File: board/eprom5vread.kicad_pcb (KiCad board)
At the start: 4 copper layers, 47 parts, among them J1 Barrel_Jack, J2 Conn_02x21_Counter_Clockwise, U1 NCP1117ST33T3G, U2 NCP1117ST50T3G, U3 TXB0108PW, U4 TXB0108PW, U5 TXB0108PW, U6 TXB0108PW, U7 TXB0108PW, U8 STM32G0B0CETx

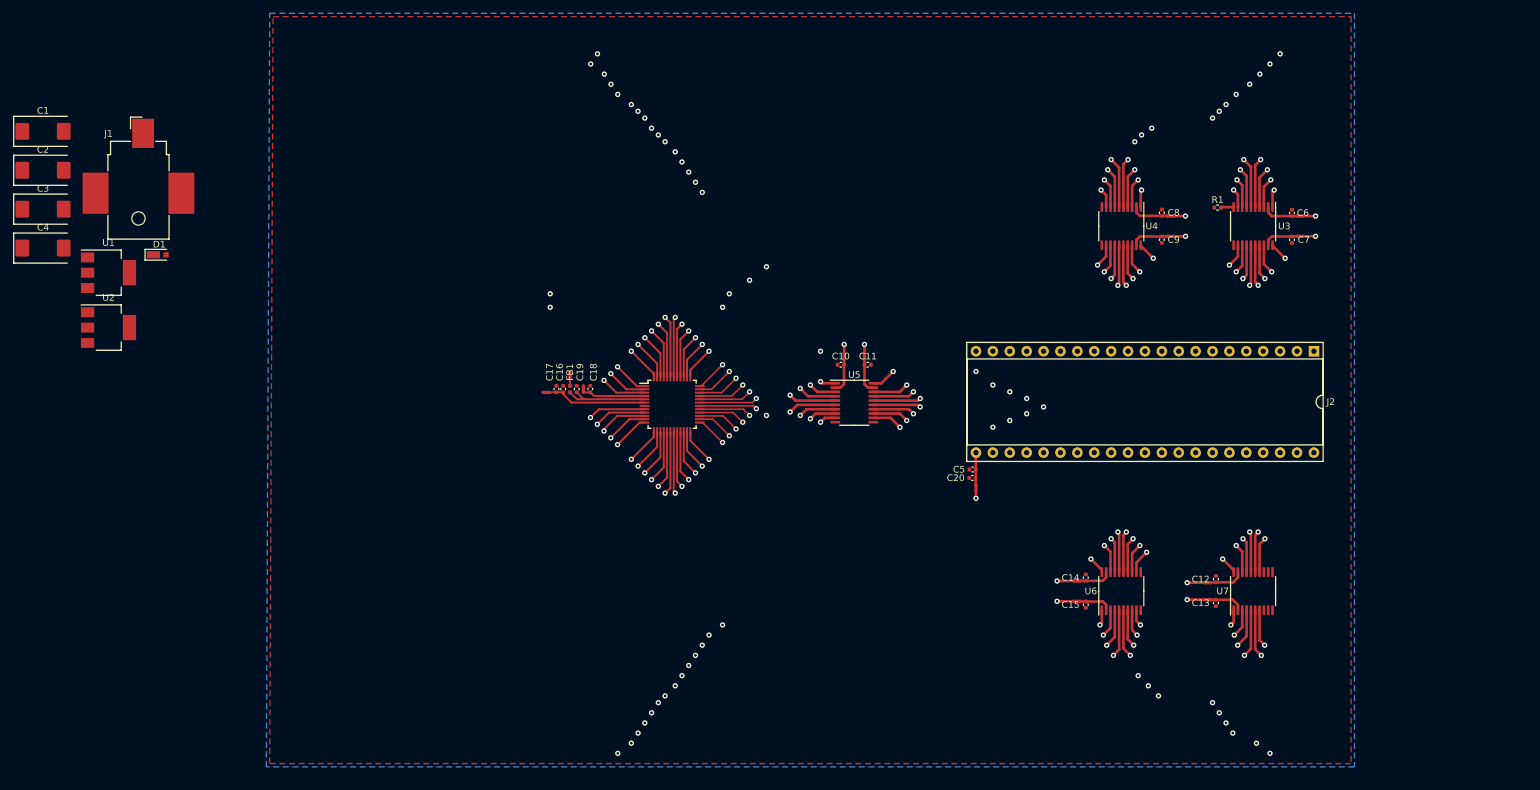
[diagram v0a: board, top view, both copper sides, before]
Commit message: initial board layout (WIP), schematic tuning
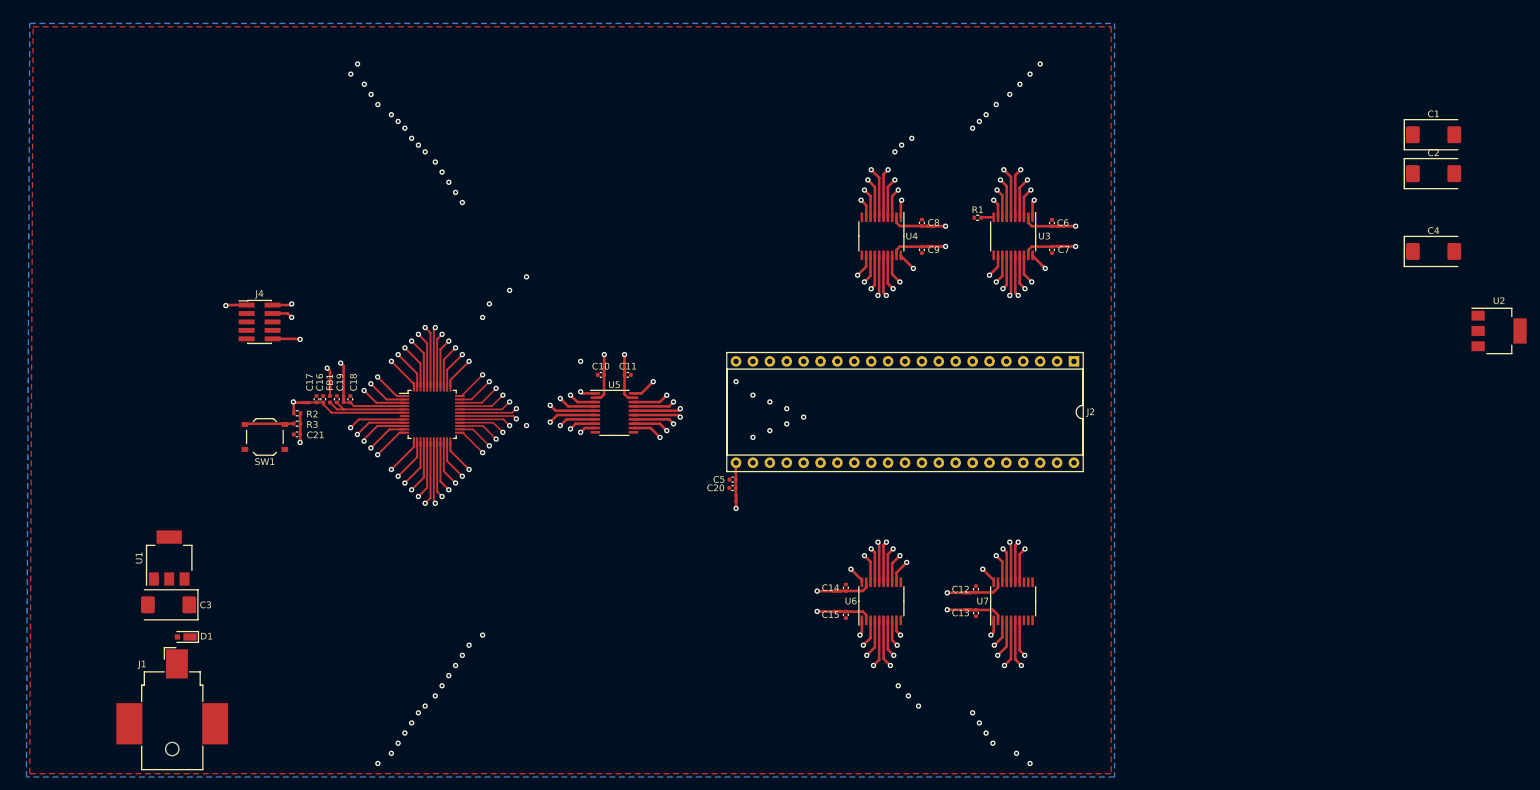
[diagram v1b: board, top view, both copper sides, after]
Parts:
- added C21: 100nF, Capacitor_SMD:C_0402_1005Metric, F.Cu at (83.3, 88.2)
- added J4: DEBUG, Connector_PinHeader_1.27mm:PinHeader_2x05_P1.27mm_Vertical_SMD, F.Cu at (77.7, 71.3)
- added R2: 2.2kΩ, Resistor_SMD:R_0402_1005Metric, F.Cu at (83.4, 85.0)
- added R3: 330Ω, Resistor_SMD:R_0402_1005Metric, F.Cu at (83.4, 86.6)
- added SW1: RST, Button_Switch_SMD:SW_Push_1P1T_XKB_TS-1187A, F.Cu at (78.5, 88.6)
- moved C1 209.0 mm to (254.2, 43.1)
- moved C2 209.0 mm to (254.2, 49.0)
- moved C4 209.0 mm to (254.2, 60.7)
- moved U2 209.0 mm to (264.1, 72.6)
- moved J1 79.9 mm to (64.6, 128.5)
- moved C3 62.4 mm to (64.0, 113.8), turned to 180 degrees
- moved D1 57.6 mm to (66.4, 118.6), turned to 180 degrees
- moved U1 43.9 mm to (64.1, 106.8), turned to 90 degrees
- moved C12 36.1 mm to (185.4, 111.5)
- moved C13 36.1 mm to (185.4, 115.1)
- moved C14 36.1 mm to (165.9, 111.3)
- moved C15 36.1 mm to (165.9, 115.3)
- moved C16 36.1 mm to (87.3, 82.9)
- moved C5 36.1 mm to (148.8, 95.0)
- moved C6 36.1 mm to (196.8, 56.4)
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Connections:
- C2 pad 1: /Power Supply/+3.3V -> /EPROM/+3.3V
- C4 pad 1: /Power Supply/+5V -> /EPROM/+5V
- NT1 pad 1: /MCU/+3.3V -> /EPROM/+3.3V
- NT2 pad 1: /MCU/+3.3V -> /EPROM/+3.3V
- NT3 pad 1: /MCU/+3.3V -> /EPROM/+3.3V
- U1 pad 2: /Power Supply/+3.3V -> /EPROM/+3.3V
- U2 pad 2: /Power Supply/+5V -> /EPROM/+5V
- U8 pad 10: unconnected-(U8-NRST-Pad10) -> /MCU/MCU Debug/~{RST}
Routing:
- net /MCU/MCU Debug/~{RST}: track 0.00 -> 40.9 mm, vias 0 -> 3
- net /EPROM/+3.3V: track 9.95 -> 23.8 mm, vias 5 -> 9
- net Net-(R3-Pad2): track 0.00 -> 7.22 mm
- net unconnected-(U8-NRST-Pad10): track 7.18 -> 0.00 mm, vias 1 -> 0
- net /MCU/SWCLK: track 39.3 -> 45.2 mm
- net /MCU/SWDIO: track 44.2 -> 49.9 mm

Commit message: finish board design
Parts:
- added J102: UART, Connector_PinHeader_2.54mm:PinHeader_2x01_P2.54mm_Vertical_SMD, F.Cu at (77.8, 58.1)
- added NT301: NetTie_2, NetTie:NetTie-2_SMD_Pad0.5mm, F.Cu at (61.5, 95.5)
- added NT302: NetTie_2, NetTie:NetTie-2_SMD_Pad0.5mm, F.Cu at (75.7, 99.1)
- added REF1: JLCPCB_Mounting_Hole, JLCPCB:JLCPCB_Mounting_Hole, F.Cu at (49.5, 32.0)
- added REF2: JLCPCB_Mounting_Hole, JLCPCB:JLCPCB_Mounting_Hole, F.Cu at (200.7, 32.0)
- added REF3: JLCPCB_Mounting_Hole, JLCPCB:JLCPCB_Mounting_Hole, F.Cu at (49.5, 134.1)
- added REF4: Polarity_Center_Positive_6mm_SilkScreen, Symbol:Polarity_Center_Positive_6mm_SilkScreen, F.Cu at (86.9, 124.2)
- moved C301 208.6 mm to (58.2, 114.6), turned to 180 degrees
- moved C302 202.3 mm to (58.2, 99.1), turned to 180 degrees
- moved U302 196.8 mm to (70.2, 106.8), turned to 90 degrees
- moved C304 188.0 mm to (70.1, 99.1), turned to 180 degrees
- moved C303 6.14 mm to (70.1, 114.6)
- moved U301 5.84 mm to (58.3, 106.8)
- moved R201 1.52 mm to (184.2, 55.6)
- renumbered C17 to C101, C16 to C102, C18 to C103, C19 to C104, C21 to C105, C6 to C201, C7 to C202, C8 to C203, C9 to C204, C10 to C205, C11 to C206, C15 to C207, C14 to C208, C13 to C209, C12 to C210, C20 to C211, C5 to C212, C1 to C301, C2 to C302, C3 to C303, C4 to C304, D1 to D301, FB1 to FB101, J4 to J101, J2 to J201, J1 to J301, NT1 to NT101, NT2 to NT102, NT3 to NT103, NT4 to NT201, NT9 to NT202, NT5 to NT203, NT10 to NT204, NT6 to NT205, NT11 to NT206, NT12 to NT207, NT8 to NT208, NT13 to NT209, NT7 to NT210, R2 to R101, R3 to R102, R1 to R201, SW1 to SW101, U8 to U101, U3 to U201, U4 to U202, U5 to U203, U6 to U204, U7 to U205, U1 to U301, U2 to U302
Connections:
- C302 pad 1: /EPROM/+3.3V -> Net-(U301-VO)
- C304 pad 1: /EPROM/+5V -> Net-(U302-VO)
- U101 pad 11: /MCU/PA0 -> /LSOE
- U301 pad 2: /EPROM/+3.3V -> Net-(U301-VO)
- U302 pad 2: /EPROM/+5V -> Net-(U302-VO)
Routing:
- net /LSOE: track 1.93 -> 264.1 mm, vias 0 -> 9
- net /EPROM/+5V: track 11.0 -> 69.5 mm, vias 6 -> 8
- net /MCU/UART_MCUTX: track 32.8 -> 82.1 mm, vias 3 -> 4
- net /MCU/UART_MCURX: track 24.7 -> 68.1 mm, vias 2 -> 3
- net Net-(D301-K): track 0.00 -> 25.2 mm
- net Net-(U301-VO): track 0.00 -> 15.2 mm
- net Net-(U302-VO): track 0.00 -> 14.0 mm
- net /MCU/PA0: track 6.21 -> 0.00 mm, vias 1 -> 0
- net Net-(D301-A): track 0.00 -> 3.97 mm
- net /EPROM/+3.3V: track 23.8 -> 25.3 mm, vias 9 -> 10
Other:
- board outline added: 161 x 112 mm
- board text added: "+3.3V"
- board text added: "+5V"
- board text added: "12V recommended"
- board text added: "EPROM 5V Read"
- board text added: "UART +3.3V"
- board text added: "r0001"
- board text added: "←MCU"
- board text added: "→MCU"

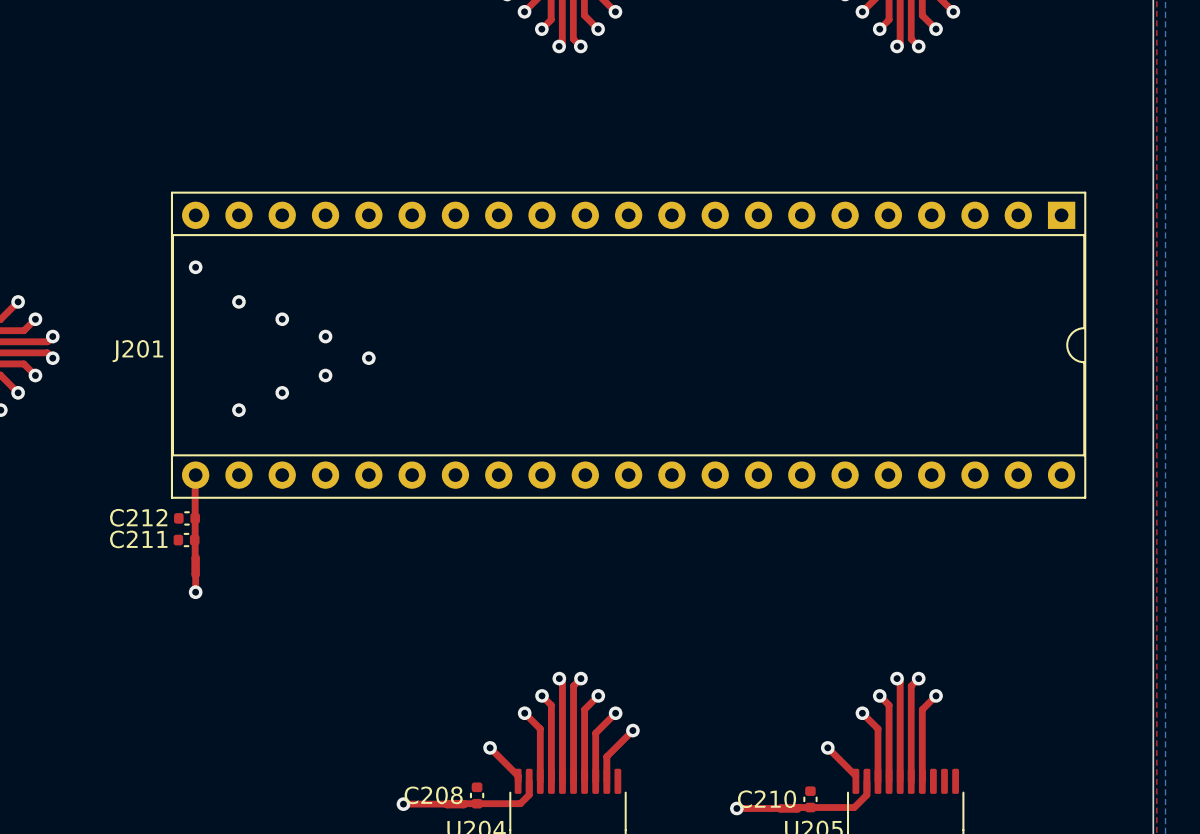
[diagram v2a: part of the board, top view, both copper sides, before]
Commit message: pcb: add ROM pin hints
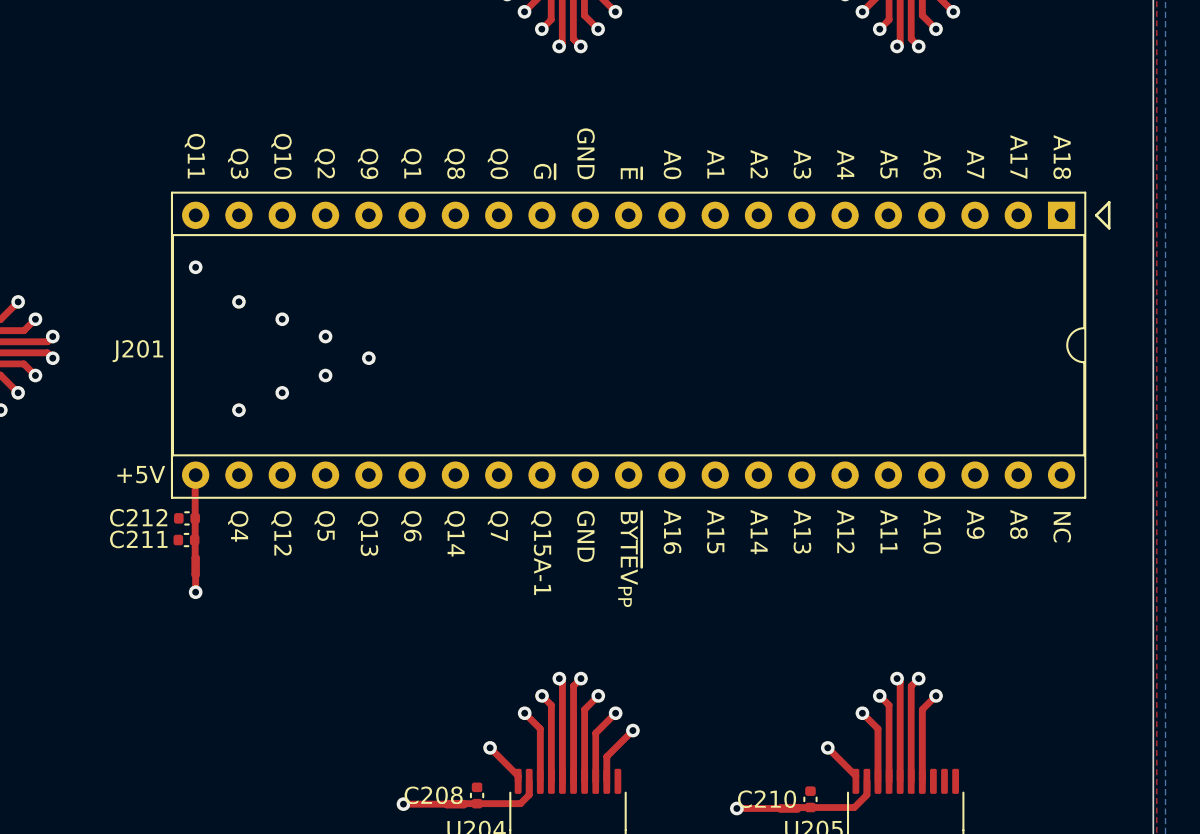
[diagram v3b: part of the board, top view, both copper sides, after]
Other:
- board text added: "A0"
- board text added: "A1"
- board text added: "A10"
- board text added: "A11"
- board text added: "A12"
- board text added: "A13"
- board text added: "A14"
- board text added: "A15"
- board text added: "A16"
- board text added: "A17"
- board text added: "A18"
- board text added: "A2"
- board text added: "A3"
- board text added: "A4"
- board text added: "A5"
- board text added: "A6"
- board text added: "A7"
- board text added: "A8"
- board text added: "A9"
- board text added: "GND"
- board text added: "NC"
- board text added: "Q0"
- board text added: "Q1"
- board text added: "Q10"
- board text added: "Q11"
- board text added: "Q12"
- board text added: "Q13"
- board text added: "Q14"
- board text added: "Q15A-1"
- board text added: "Q2"
- board text added: "Q3"
- board text added: "Q4"
- board text added: "Q5"
- board text added: "Q6"
- board text added: "Q7"
- board text added: "Q8"
- board text added: "Q9"
- board text added: "~{BYTE}V_{PP}"
- board text added: "~{E}"
- board text added: "~{G}"
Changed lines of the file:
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@@
     )
   )
+  (gr_poly
+    (pts
+      (xy 202.184 77.216)
+      (xy 202.946 76.454)
+      (xy 202.946 77.978)
+    )
+    (stroke (width 0.15) (type solid)) (fill none) (layer "F.SilkS"))
   (gr_line (start 49.532 139.092) (end 200.532 139.092)
     (stroke (width 0.1) (type default)) (layer "Edge.Cuts"))
@@
   (gr_arc (start 44.532 32.092) (mid 45.996466 28.556466) (end 49.532 27.092)
     (stroke (width 0.1) (type default)) (layer "Edge.Cuts"))
+  (gr_text "A3" (at 184.912 75.184 270) (layer "F.SilkS")
+    (effects (font (size 1 1) (thickness 0.15)) (justify right))
+  )
   (gr_text "12V recommended" (at 86.868 130.302) (layer "F.SilkS")
     (effects (font (size 1.8 1.8) (thickness 0.25)) (justify bottom))
   )
+  (gr_text "Q6" (at 162.052 94.488 270) (layer "F.SilkS")
+    (effects (font (size 1 1) (thickness 0.15)) (justify left))
+  )
+  (gr_text "Q0" (at 167.132 75.184 270) (layer "F.SilkS")
+    (effects (font (size 1 1) (thickness 0.15)) (justify right))
+  )
+  (gr_text "A8" (at 197.612 94.488 270) (layer "F.SilkS")
+    (effects (font (size 1 1) (thickness 0.15)) (justify left))
+  )
+  (gr_text "A9" (at 195.072 94.488 270) (layer "F.SilkS")
+    (effects (font (size 1 1) (thickness 0.15)) (justify left))
+  )
+  (gr_text "Q12" (at 154.432 94.488 270) (layer "F.SilkS")
+    (effects (font (size 1 1) (thickness 0.15)) (justify left))
+  )
+  (gr_text "A10" (at 192.532 94.488 270) (layer "F.SilkS")
+    (effects (font (size 1 1) (thickness 0.15)) (justify left))
+  )
+  (gr_text "A2" (at 182.372 75.184 270) (layer "F.SilkS")
+    (effects (font (size 1 1) (thickness 0.15)) (justify right))
+  )
+  (gr_text "Q5" (at 156.972 94.488 270) (layer "F.SilkS")
+    (effects (font (size 1 1) (thickness 0.15)) (justify left))
+  )
+  (gr_text "Q7" (at 167.132 94.488 270) (layer "F.SilkS")
+    (effects (font (size 1 1) (thickness 0.15)) (justify left))
+  )
+  (gr_text "GND" (at 172.212 94.488 270) (layer "F.SilkS")
+    (effects (font (size 1 1) (thickness 0.15)) (justify left))
+  )
+  (gr_text "A0" (at 177.292 75.184 270) (layer "F.SilkS")
+    (effects (font (size 1 1) (thickness 0.15)) (justify right))
+  )
+  (gr_text "Q2" (at 156.972 75.184 270) (layer "F.SilkS")
+    (effects (font (size 1 1) (thickness 0.15)) (justify right))
+  )
+  (gr_text "A16" (at 177.292 94.488 270) (layer "F.SilkS")
+    (effects (font (size 1 1) (thickness 0.15)) (justify left))
+  )
+  (gr_text "Q13" (at 159.512 94.488 270) (layer "F.SilkS")
+    (effects (font (size 1 1) (thickness 0.15)) (justify left))
+  )
+  (gr_text "A7" (at 195.072 75.184 270) (layer "F.SilkS")
+    (effects (font (size 1 1) (thickness 0.15)) (justify right))
+  )
+  (gr_text "Q3" (at 151.892 75.184 270) (layer "F.SilkS")
+    (effects (font (size 1 1) (thickness 0.15)) (justify right))
+  )
+  (gr_text "Q10" (at 154.432 75.184 270) (layer "F.SilkS")
+    (effects (font (size 1 1) (thickness 0.15)) (justify right))
+  )
+  (gr_text "Q4" (at 151.892 94.488 270) (layer "F.SilkS")
+    (effects (font (size 1 1) (thickness 0.15)) (justify left))
+  )
+  (gr_text "A11" (at 189.992 94.488 270) (layer "F.SilkS")
+    (effects (font (size 1 1) (thickness 0.15)) (justify left))
+  )
+  (gr_text "A6" (at 192.532 75.184 270) (layer "F.SilkS")
+    (effects (font (size 1 1) (thickness 0.15)) (justify right))
+  )
+  (gr_text "A15" (at 179.832 94.488 270) (layer "F.SilkS")
+    (effects (font (size 1 1) (thickness 0.15)) (justify left))
+  )
+  (gr_text "A18" (at 200.152 75.184 -90) (layer "F.SilkS")
+    (effects (font (size 1 1) (thickness 0.15)) (justify right))
+  )
+  (gr_text "Q9" (at 159.512 75.184 270) (layer "F.SilkS")
+    (effects (font (size 1 1) (thickness 0.15)) (justify right))
+  )
+  (gr_text "+5V" (at 147.574 92.456) (layer "F.SilkS")
+    (effects (font (size 1 1) (thickness 0.15)) (justify right))
+  )
+  (gr_text "NC" (at 200.152 94.488 270) (layer "F.SilkS")
+    (effects (font (size 1 1) (thickness 0.15)) (justify left))
+  )
   (gr_text "←MCU" (at 75.104 57.362) (layer "F.SilkS")
     (effects (font (size 1 1) (thickness 0.15)) (justify right bottom))
   )
+  (gr_text "Q8" (at 164.592 75.184 270) (layer "F.SilkS")
+    (effects (font (size 1 1) (thickness 0.15)) (justify right))
+  )
+  (gr_text "A14" (at 182.372 94.488 270) (layer "F.SilkS")
+    (effects (font (size 1 1) (thickness 0.15)) (justify left))
+  )
+  (gr_text "A5" (at 189.992 75.184 270) (layer "F.SilkS")
+    (effects (font (size 1 1) (thickness 0.15)) (justify right))
+  )
+  (gr_text "Q11" (at 149.352 75.184 270) (layer "F.SilkS")
+    (effects (font (size 1 1) (thickness 0.15)) (justify right))
+  )
+  (gr_text "~{E}" (at 174.752 75.184 270) (layer "F.SilkS")
+    (effects (font (size 1 1) (thickness 0.15)) (justify right))
+  )
+  (gr_text "Q15A-1" (at 169.672 94.488 270) (layer "F.SilkS")
+    (effects (font (size 1 1) (thickness 0.15)) (justify left))
+  )
+  (gr_text "A17" (at 197.612 75.184 270) (layer "F.SilkS")
+    (effects (font (size 1 1) (thickness 0.15)) (justify right))
+  )
+  (gr_text "Q1" (at 162.052 75.184 270) (layer "F.SilkS")
+    (effects (font (size 1 1) (thickness 0.15)) (justify right))
+  )
+  (gr_text "GND" (at 172.212 75.184 270) (layer "F.SilkS")
+    (effects (font (size 1 1) (thickness 0.15)) (justify right))
+  )
+  (gr_text "Q14" (at 164.592 94.488 270) (layer "F.SilkS")
+    (effects (font (size 1 1) (thickness 0.15)) (justify left))
+  )
   (gr_text "UART\n+3.3V" (at 70.024 59.568) (layer "F.SilkS")
     (effects (font (size 1 1) (thickness 0.15)) (justify right bottom))
   )
+  (gr_text "A4" (at 187.452 75.184 270) (layer "F.SilkS")
+    (effects (font (size 1 1) (thickness 0.15)) (justify right))
+  )
+  (gr_text "~{BYTE}V_{PP}" (at 174.752 94.488 270) (layer "F.SilkS")
+    (effects (font (size 1 1) (thickness 0.15)) (justify left))
+  )
+  (gr_text "A1" (at 179.832 75.184 270) (layer "F.SilkS")
+    (effects (font (size 1 1) (thickness 0.15)) (justify right))
+  )
+  (gr_text "A12" (at 187.452 94.488 270) (layer "F.SilkS")
+    (effects (font (size 1 1) (thickness 0.15)) (justify left))
+  )
   (gr_text "→MCU" (at 75.104 59.822) (layer "F.SilkS")
     (effects (font (size 1 1) (thickness 0.15)) (justify right bottom))
+  )
+  (gr_text "A13" (at 184.912 94.488 270) (layer "F.SilkS")
+    (effects (font (size 1 1) (thickness 0.15)) (justify left))
   )
   (gr_text "EPROM\n5V Read" (at 59.944 44.704) (layer "F.SilkS")
@@
     (effects (font (size 1 1) (thickness 0.15)) (justify bottom))
   )
+  (gr_text "~{G}" (at 169.672 75.184 270) (layer "F.SilkS")
+    (effects (font (size 1 1) (thickness 0.15)) (justify right))
+  )
   (gr_text "+3.3V" (at 58.42 95.758) (layer "F.Fab")
